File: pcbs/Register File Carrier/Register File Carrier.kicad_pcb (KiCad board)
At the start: 2 copper layers, 238.8 x 213.4 mm, 95 parts, among them J1001 Conn_02x20_Odd_Even, J1002 Conn_02x20_Odd_Even, U2001 74AHC04, U3001 74HC14, U3002 74HC08, U3003 74HC138, U3004 74HC08, U4001 74HC245, U4002 74HC245, U5001 74HC245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

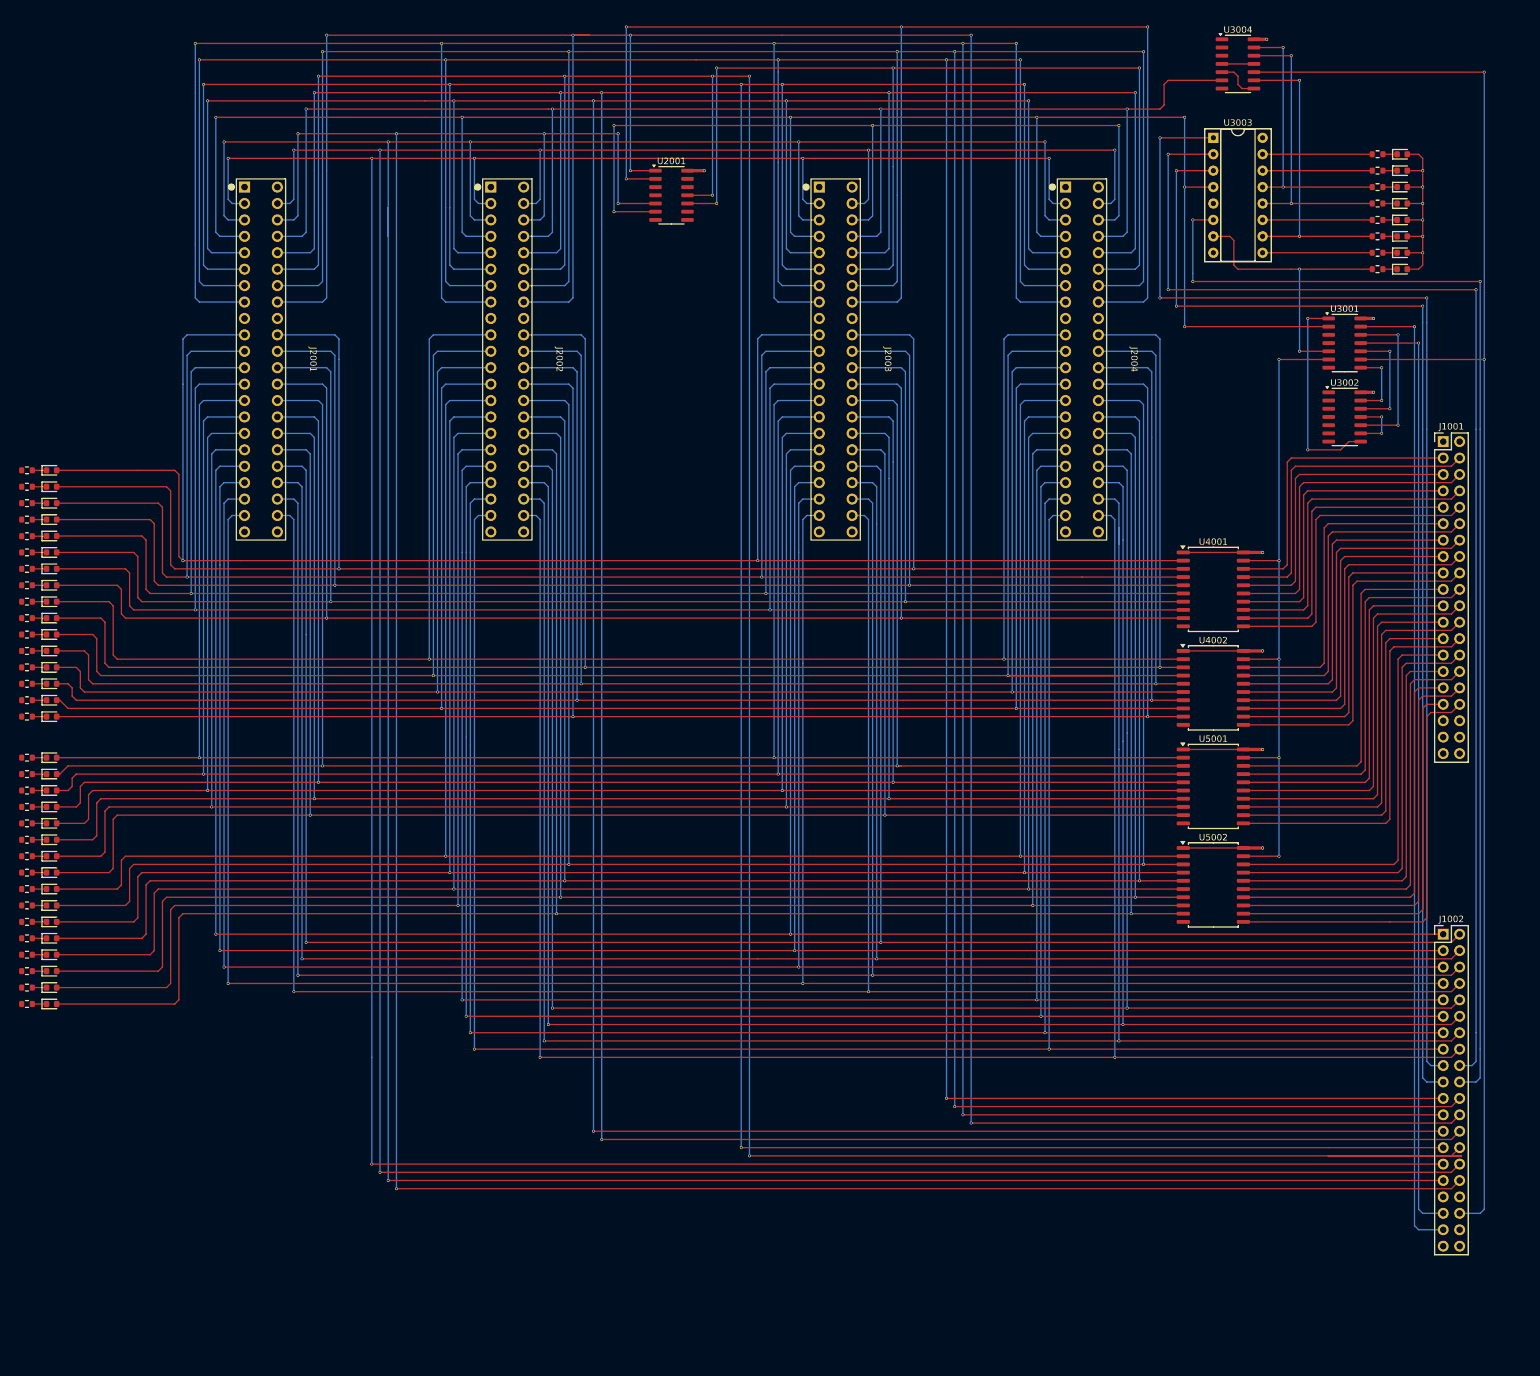
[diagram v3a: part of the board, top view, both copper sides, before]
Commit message: Adding mounting holes; thinking about needs
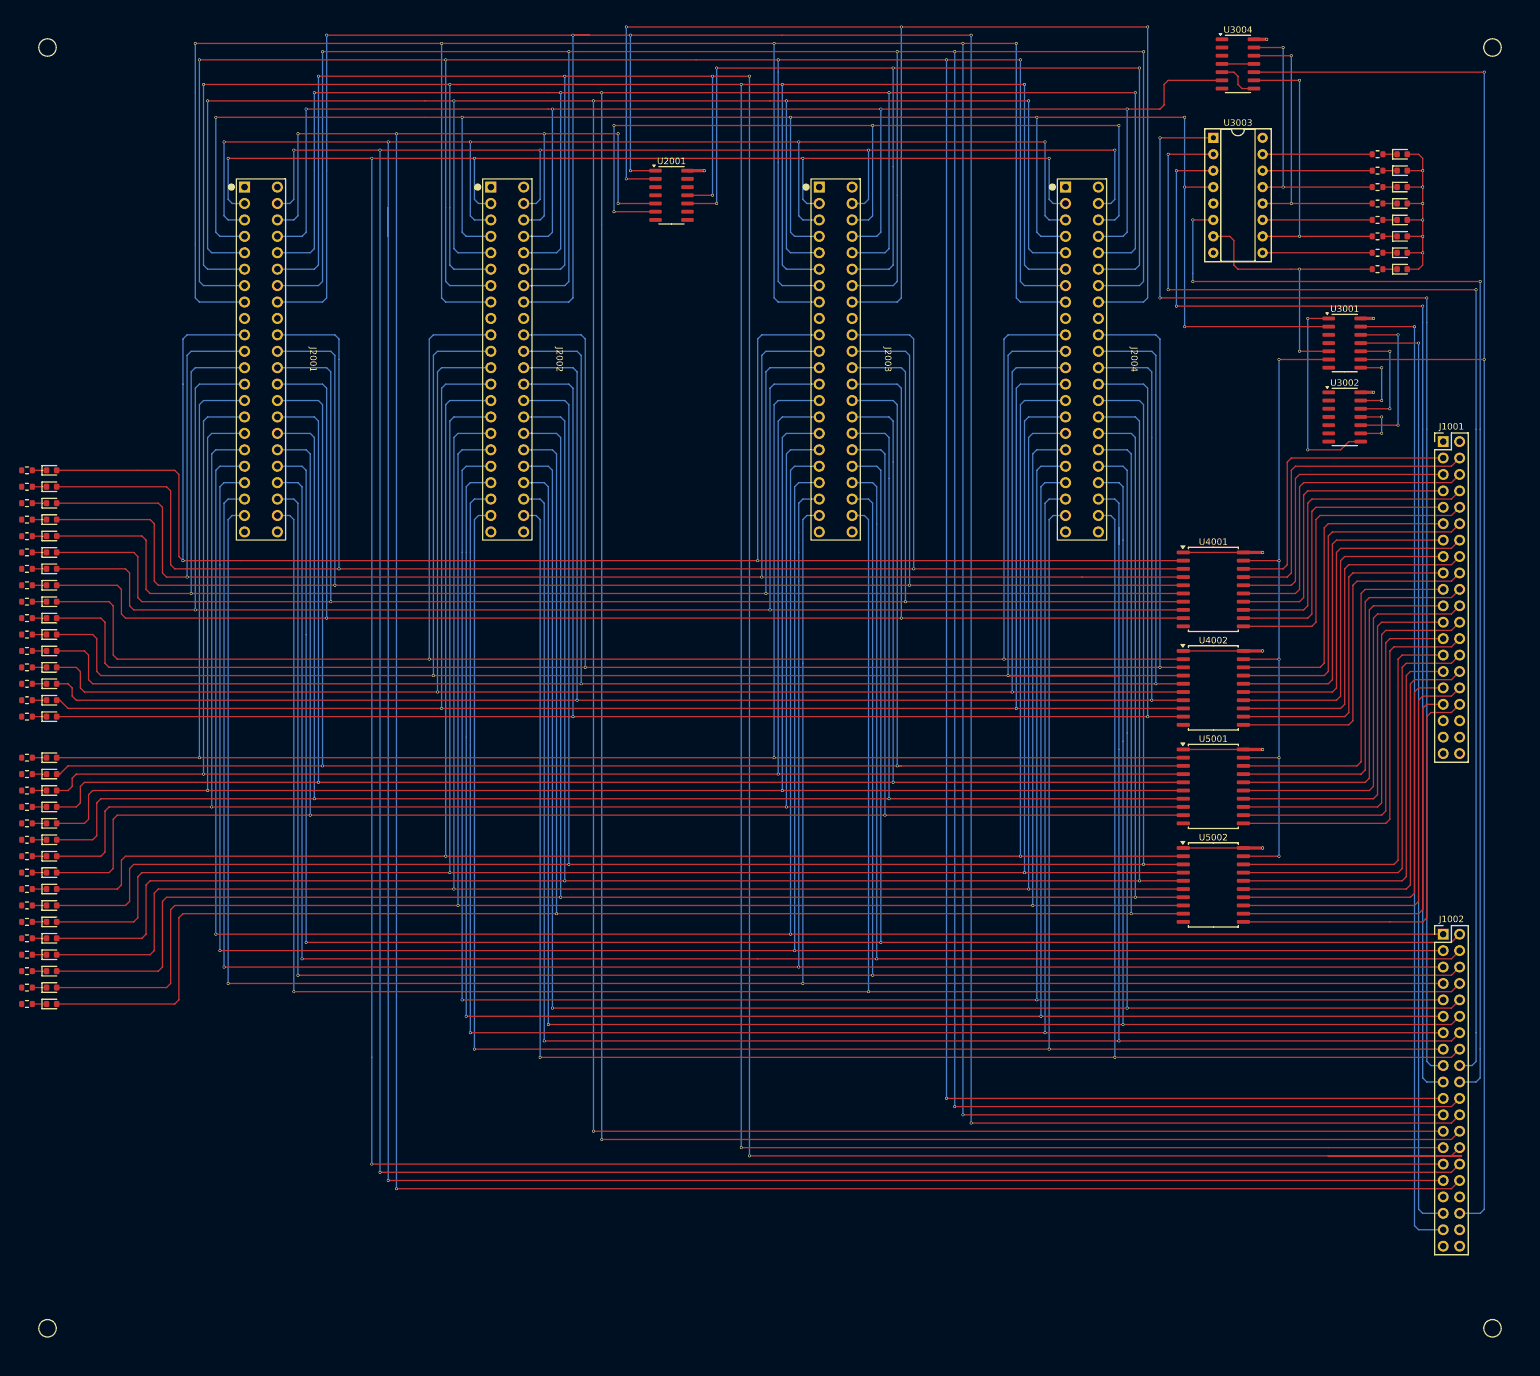
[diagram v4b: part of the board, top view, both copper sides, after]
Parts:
- added H1001: MountingHole, MountingHole:MountingHole_2.7mm_M2.5_ISO7380, F.Cu at (68.6, 53.3)
- added H1002: MountingHole, MountingHole:MountingHole_2.7mm_M2.5_ISO7380, F.Cu at (292.1, 53.3)
- added H1003: MountingHole, MountingHole:MountingHole_2.7mm_M2.5_ISO7380, F.Cu at (68.6, 251.5)
- added H1004: MountingHole, MountingHole:MountingHole_2.7mm_M2.5_ISO7380, F.Cu at (292.1, 251.5)

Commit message: Shrink board slightly
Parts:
- added C3001: 100n, Capacitor_SMD:C_0603_1608Metric, F.Cu at (259.7, 52.1)
- moved H1004 5.68 mm to (289.6, 246.4)
- moved H1003 5.08 mm to (68.6, 246.4)
- moved H1002 3.59 mm to (289.6, 55.9)
- moved H1001 2.54 mm to (68.6, 55.9)
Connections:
- U3003 pad 5: unconnected-(U3003-~{E1}-Pad5) -> GND
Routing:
- net +5V: track 93.7 -> 95.5 mm
- net /Cycle3: track 234.7 -> 234.0 mm
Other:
- board size 238.8 x 213.4 mm -> 236.2 x 205.7 mm

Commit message: Silkscreen
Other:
- board text added: "+5V"
- board text added: "A0"
- board text added: "A10"
- board text added: "A12"
- board text added: "A14"
- board text added: "A2"
- board text added: "A4"
- board text added: "A6"
- board text added: "A8"
- board text added: "B0"
- board text added: "B10"
- board text added: "B12"
- board text added: "B14"
- board text added: "B2"
- board text added: "B4"
- board text added: "B6"
- board text added: "B8"
- board text added: "BRANCHZERO"
- board text added: "GND"
- board text added: "HALT"
- board text added: "LOADB"
- board text added: "LOADPC"
- board text added: "LOADW"
- board text added: "RGE2025"
- board text added: "Register File"
- board text added: "Registers 0-7"
- board text added: "Registers 8-15"
- board text added: "SET"
- board text added: "STOREB"
- board text added: "STOREW"

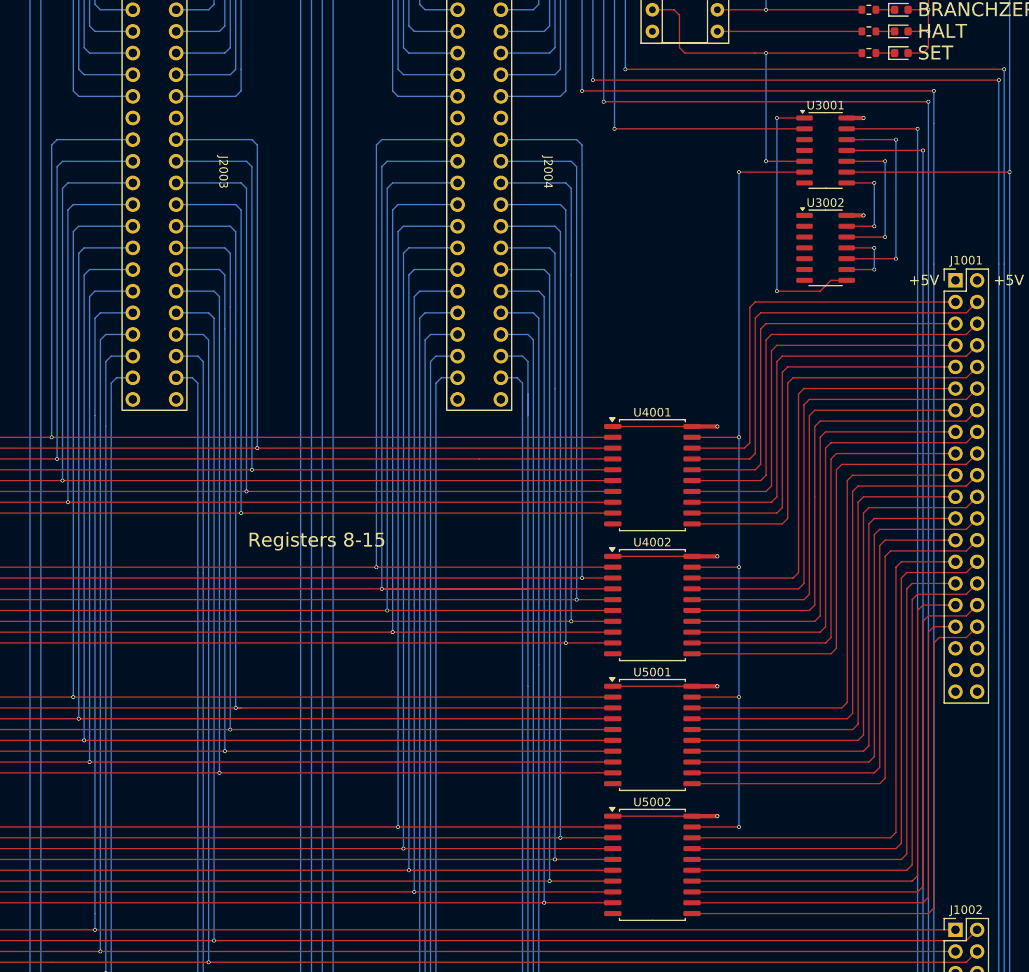
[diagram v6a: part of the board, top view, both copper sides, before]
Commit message: Rerouting
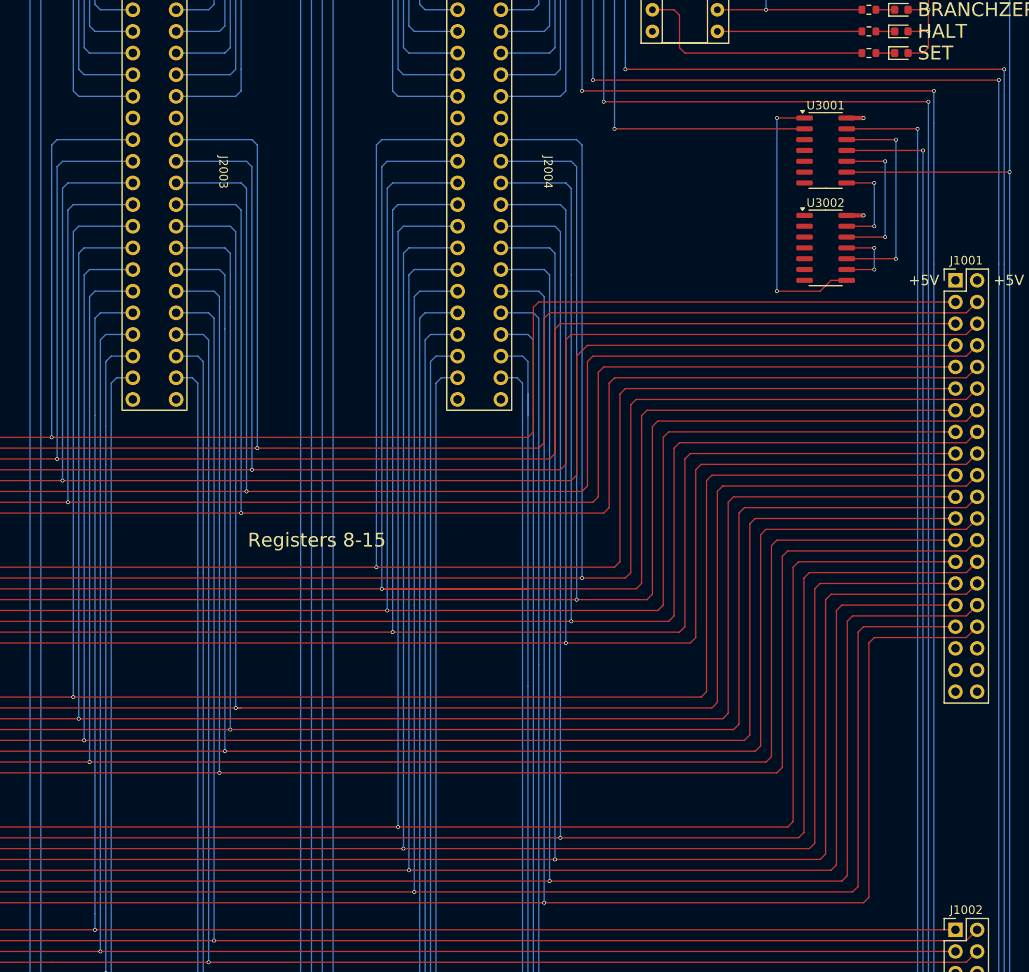
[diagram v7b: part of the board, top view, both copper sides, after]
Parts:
- removed U4001, U4002, U5001, U5002: 74HC245, Package_SO:SOIC-20W_7.5x12.8mm_P1.27mm
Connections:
- D4001 pad 2: /Connector Block/A0 -> /Ao0
- D4002 pad 2: /Connector Block/A1 -> /Ao1
- D4003 pad 2: /Connector Block/A2 -> /Ao2
- D4004 pad 2: /Connector Block/A3 -> /Ao3
- D4005 pad 2: /Connector Block/A4 -> /Ao4
- D4006 pad 2: /Connector Block/A5 -> /Ao5
- D4007 pad 2: /Connector Block/A6 -> /Ao6
- D4008 pad 2: /Connector Block/A7 -> /Ao7
- D4009 pad 2: /Connector Block/A8 -> /Ao8
- D4010 pad 2: /Connector Block/A9 -> /Ao9
- D4011 pad 2: /Connector Block/A10 -> /Ao10
- D4012 pad 2: /Connector Block/A11 -> /Ao11
- D4013 pad 2: /Connector Block/A12 -> /Ao12
- D4014 pad 2: /Connector Block/A13 -> /Ao13
- D4015 pad 2: /Connector Block/A14 -> /Ao14
- D4016 pad 2: /Connector Block/A15 -> /Ao15
- D5001 pad 2: /Connector Block/B0 -> /Bo0
- D5002 pad 2: /Connector Block/B1 -> /Bo1
- D5003 pad 2: /Connector Block/B2 -> /Bo2
- D5004 pad 2: /Connector Block/B3 -> /Bo3
- D5005 pad 2: /Connector Block/B4 -> /Bo4
- D5006 pad 2: /Connector Block/B5 -> /Bo5
- D5007 pad 2: /Connector Block/B6 -> /Bo6
- D5008 pad 2: /Connector Block/B7 -> /Bo7
- D5009 pad 2: /Connector Block/B8 -> /Bo8
- D5010 pad 2: /Connector Block/B9 -> /Bo9
- D5011 pad 2: /Connector Block/B10 -> /Bo10
- D5012 pad 2: /Connector Block/B11 -> /Bo11
- D5013 pad 2: /Connector Block/B12 -> /Bo12
- D5014 pad 2: /Connector Block/B13 -> /Bo13
- D5015 pad 2: /Connector Block/B14 -> /Bo14
- D5016 pad 2: /Connector Block/B15 -> /Bo15
- J2001 pad A10: /Connector Block/A0 -> /Ao0
- J2001 pad A11: /Connector Block/A2 -> /Ao2
- J2001 pad A12: /Connector Block/A4 -> /Ao4
- J2001 pad A13: /Connector Block/A6 -> /Ao6
- J2001 pad A14: /Connector Block/B0 -> /Bo0
- J2001 pad A15: /Connector Block/B2 -> /Bo2
- J2001 pad A16: /Connector Block/B4 -> /Bo4
- J2001 pad A17: /Connector Block/B6 -> /Bo6
- J2001 pad B10: /Connector Block/A1 -> /Ao1
- J2001 pad B11: /Connector Block/A3 -> /Ao3
- J2001 pad B12: /Connector Block/A5 -> /Ao5
- J2001 pad B13: /Connector Block/A7 -> /Ao7
- J2001 pad B14: /Connector Block/B1 -> /Bo1
- J2001 pad B15: /Connector Block/B3 -> /Bo3
- J2001 pad B16: /Connector Block/B5 -> /Bo5
- J2001 pad B17: /Connector Block/B7 -> /Bo7
- J2002 pad A10: /Connector Block/A8 -> /Ao8
- J2002 pad A11: /Connector Block/A10 -> /Ao10
- J2002 pad A12: /Connector Block/A12 -> /Ao12
- J2002 pad A13: /Connector Block/A14 -> /Ao14
- J2002 pad A14: /Connector Block/B8 -> /Bo8
- J2002 pad A15: /Connector Block/B10 -> /Bo10
- J2002 pad A16: /Connector Block/B12 -> /Bo12
- J2002 pad A17: /Connector Block/B14 -> /Bo14
- J2002 pad B10: /Connector Block/A9 -> /Ao9
- J2002 pad B11: /Connector Block/A11 -> /Ao11
- J2002 pad B12: /Connector Block/A13 -> /Ao13
- J2002 pad B13: /Connector Block/A15 -> /Ao15
- J2002 pad B14: /Connector Block/B9 -> /Bo9
- J2002 pad B15: /Connector Block/B11 -> /Bo11
- J2002 pad B16: /Connector Block/B13 -> /Bo13
- J2002 pad B17: /Connector Block/B15 -> /Bo15
- J2003 pad A10: /Connector Block/A0 -> /Ao0
- J2003 pad A11: /Connector Block/A2 -> /Ao2
- J2003 pad A12: /Connector Block/A4 -> /Ao4
- J2003 pad A13: /Connector Block/A6 -> /Ao6
- J2003 pad A14: /Connector Block/B0 -> /Bo0
- J2003 pad A15: /Connector Block/B2 -> /Bo2
- J2003 pad A16: /Connector Block/B4 -> /Bo4
- J2003 pad A17: /Connector Block/B6 -> /Bo6
- J2003 pad B10: /Connector Block/A1 -> /Ao1
- J2003 pad B11: /Connector Block/A3 -> /Ao3
- J2003 pad B12: /Connector Block/A5 -> /Ao5
- J2003 pad B13: /Connector Block/A7 -> /Ao7
- J2003 pad B14: /Connector Block/B1 -> /Bo1
- J2003 pad B15: /Connector Block/B3 -> /Bo3
- J2003 pad B16: /Connector Block/B5 -> /Bo5
- J2003 pad B17: /Connector Block/B7 -> /Bo7
- J2004 pad A10: /Connector Block/A8 -> /Ao8
- J2004 pad A11: /Connector Block/A10 -> /Ao10
- J2004 pad A12: /Connector Block/A12 -> /Ao12
- J2004 pad A13: /Connector Block/A14 -> /Ao14
- J2004 pad A14: /Connector Block/B8 -> /Bo8
- J2004 pad A15: /Connector Block/B10 -> /Bo10
- J2004 pad A16: /Connector Block/B12 -> /Bo12
- J2004 pad A17: /Connector Block/B14 -> /Bo14
- J2004 pad B10: /Connector Block/A9 -> /Ao9
- J2004 pad B11: /Connector Block/A11 -> /Ao11
- J2004 pad B12: /Connector Block/A13 -> /Ao13
- J2004 pad B13: /Connector Block/A15 -> /Ao15
- J2004 pad B14: /Connector Block/B9 -> /Bo9
- J2004 pad B15: /Connector Block/B11 -> /Bo11
- J2004 pad B16: /Connector Block/B13 -> /Bo13
- J2004 pad B17: /Connector Block/B15 -> /Bo15
- U3001 pad 5: /Enabler/~{Set} -> GND
- U3001 pad 6: /Enabler/~{AB_{Enable}} -> unconnected-(U3001-Pad6)
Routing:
- net /Bo15: track 65.6 -> 414.1 mm, vias 0 -> 2
- net /Bo13: track 65.6 -> 412.8 mm, vias 0 -> 2
- net /Bo11: track 65.6 -> 411.5 mm, vias 0 -> 2
- net /Bo9: track 65.6 -> 410.3 mm, vias 0 -> 2
- net /Bo14: track 62.6 -> 407.2 mm, vias 0 -> 2
- net /Bo12: track 62.6 -> 405.9 mm, vias 0 -> 2
- net /Bo10: track 62.6 -> 404.7 mm, vias 0 -> 2
- net /Bo8: track 62.6 -> 403.4 mm, vias 0 -> 2
- net /Connector Block/B15: track 340.4 -> 0.00 mm, vias 2 -> 0
- net /Connector Block/B13: track 339.1 -> 0.00 mm, vias 2 -> 0
- net /Connector Block/B11: track 337.9 -> 0.00 mm, vias 2 -> 0
- net /Connector Block/B9: track 336.6 -> 0.00 mm, vias 2 -> 0
- net /Connector Block/B14: track 336.6 -> 0.00 mm, vias 2 -> 0
- net /Connector Block/B12: track 335.3 -> 0.00 mm, vias 2 -> 0
- net /Connector Block/B10: track 334.1 -> 0.00 mm, vias 2 -> 0
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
